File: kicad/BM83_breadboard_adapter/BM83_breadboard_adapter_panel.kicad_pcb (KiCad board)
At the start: 2 copper layers, 76.2 x 99.1 mm, 130 parts, among them J1 PJ-320B, J2 PJ-320B, J3 USB_B_Micro, J4 Conn_01x25_Female, J5 Conn_01x25_Female, J6 PJ-320B, SW1 VOL-, SW2 VOL+, SW3 PREV, SW4 NEXT, SW6 PLAY, SW7 SELECT, SW8 MFB, SW9 RESET, U1 BM83, U2 PJ-3027F

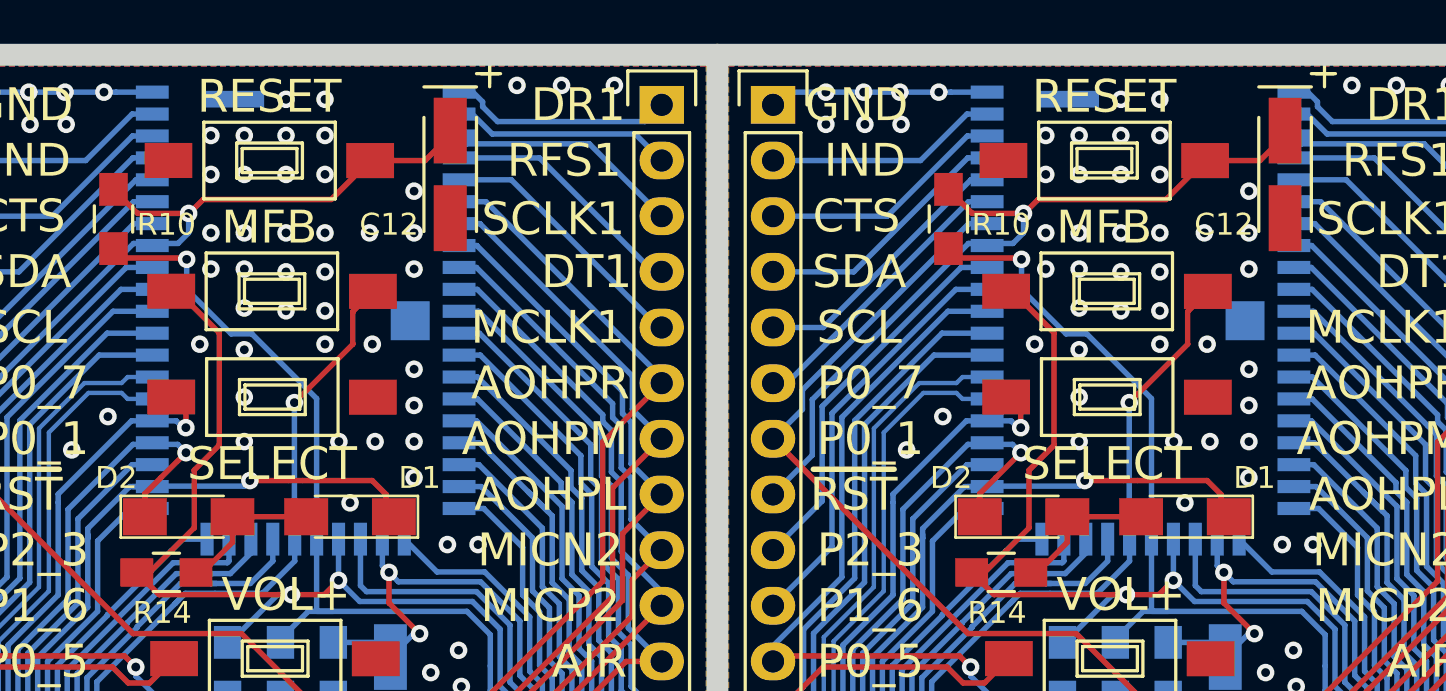
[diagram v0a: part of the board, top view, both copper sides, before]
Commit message: update BM83 footprint on board!
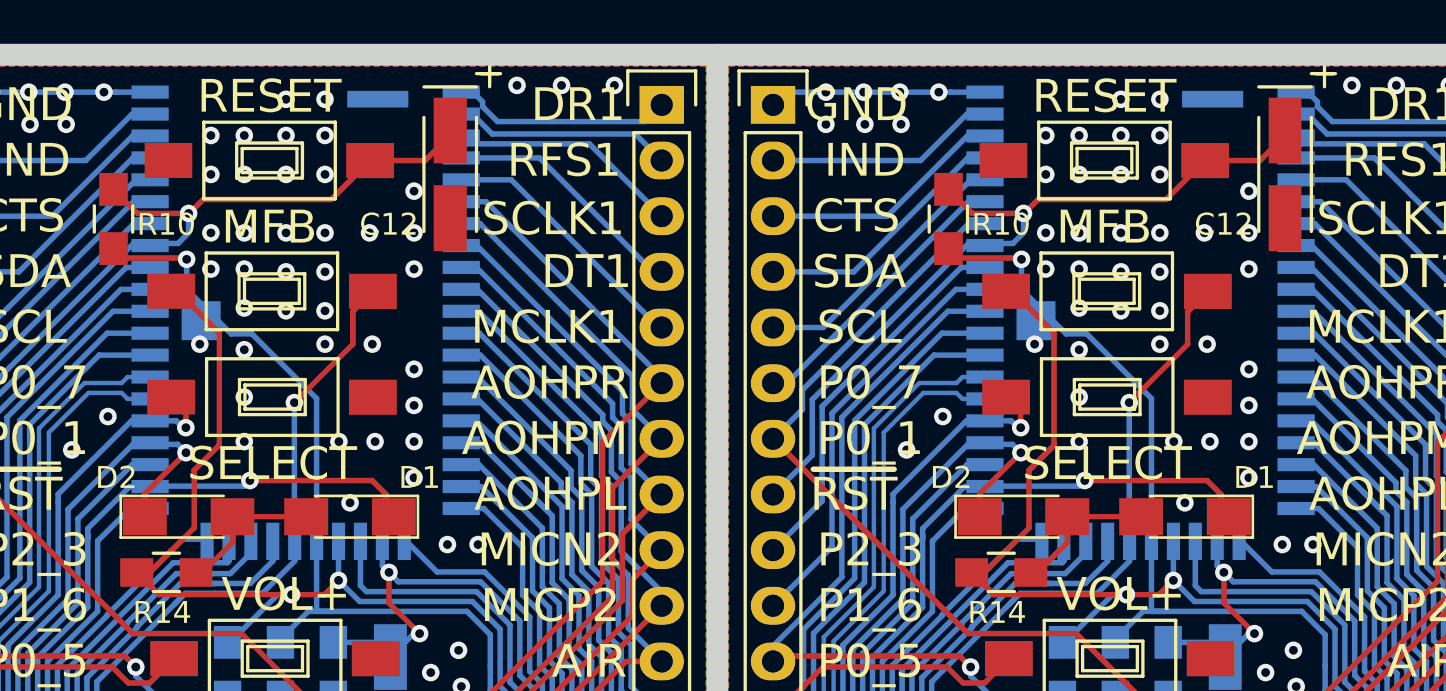
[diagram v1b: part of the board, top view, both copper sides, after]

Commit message: fixies
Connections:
- net /~RST renamed /~{RST}
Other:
- net class Default removed
- board text added: "~{RST}"
- board text removed: "~RST"
